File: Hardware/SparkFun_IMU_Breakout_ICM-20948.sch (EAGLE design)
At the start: 37 parts, among them U1 -VFQFN_20, U2 9DoF IMU, U3 1.8V/100mA

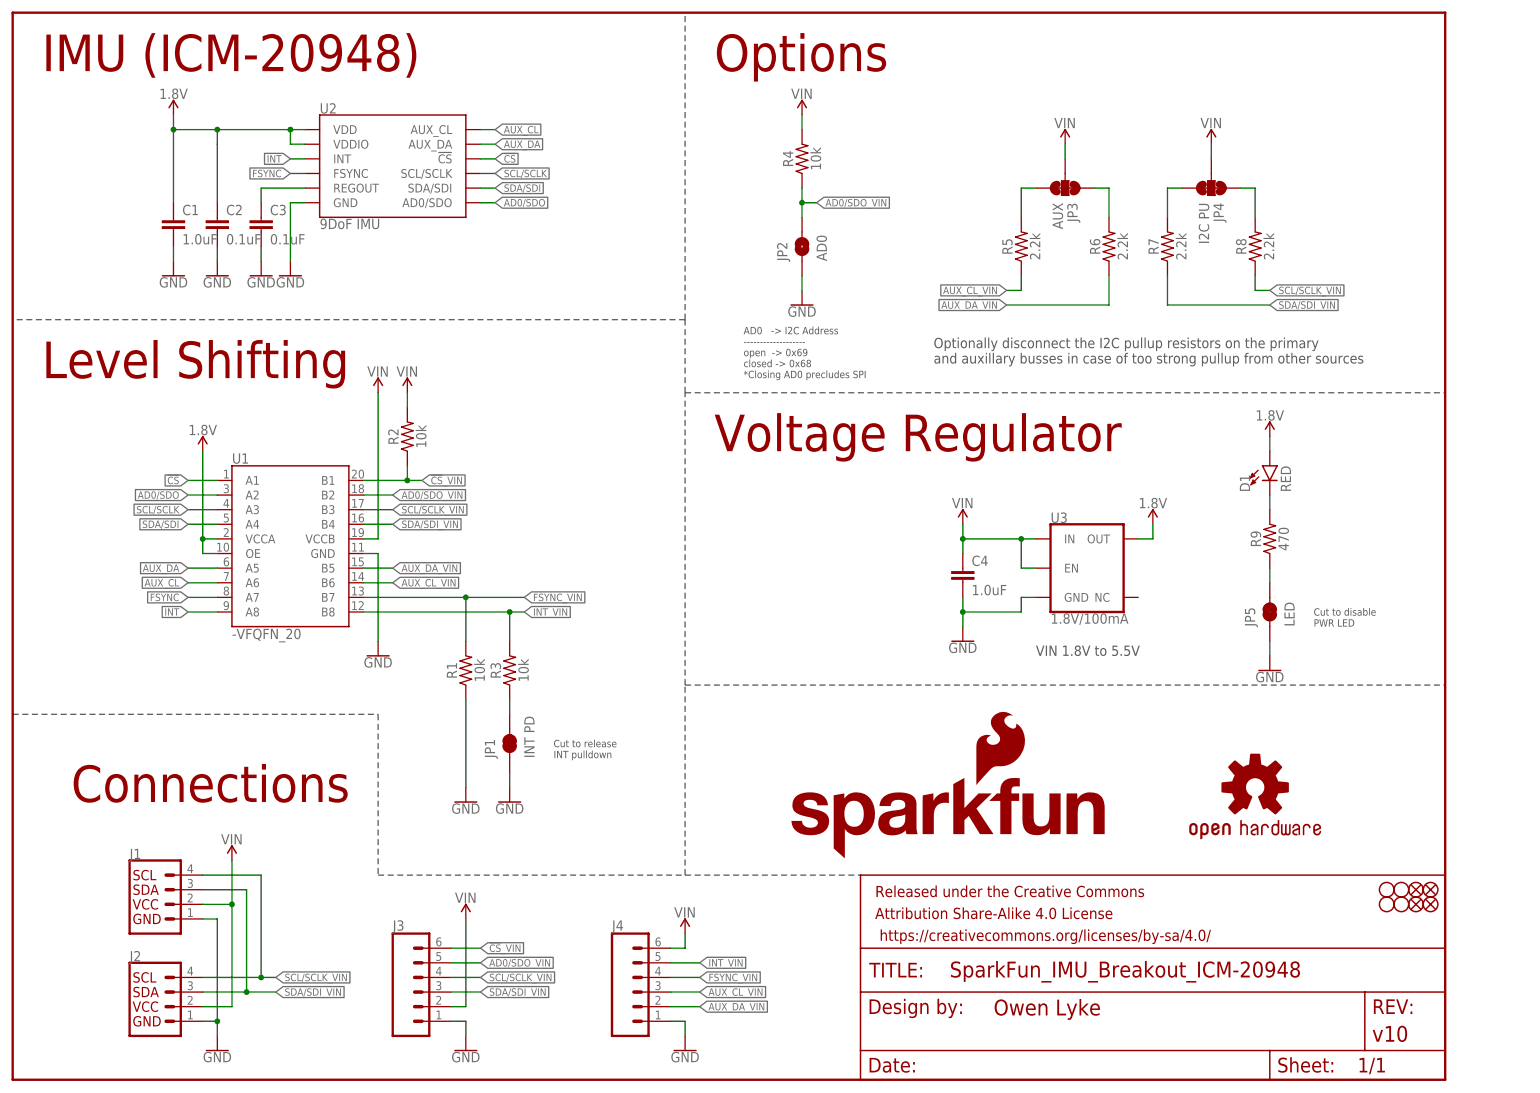
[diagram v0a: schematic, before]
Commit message: v20
v20 is intended to fix the I2C communications. We've identified that the TXB0108 logic level translation IC was unable to drive open-drain busses. To address this we've replaced that IC with the TXS0108 - a very similar chip that IS able to drive open-drain busses.
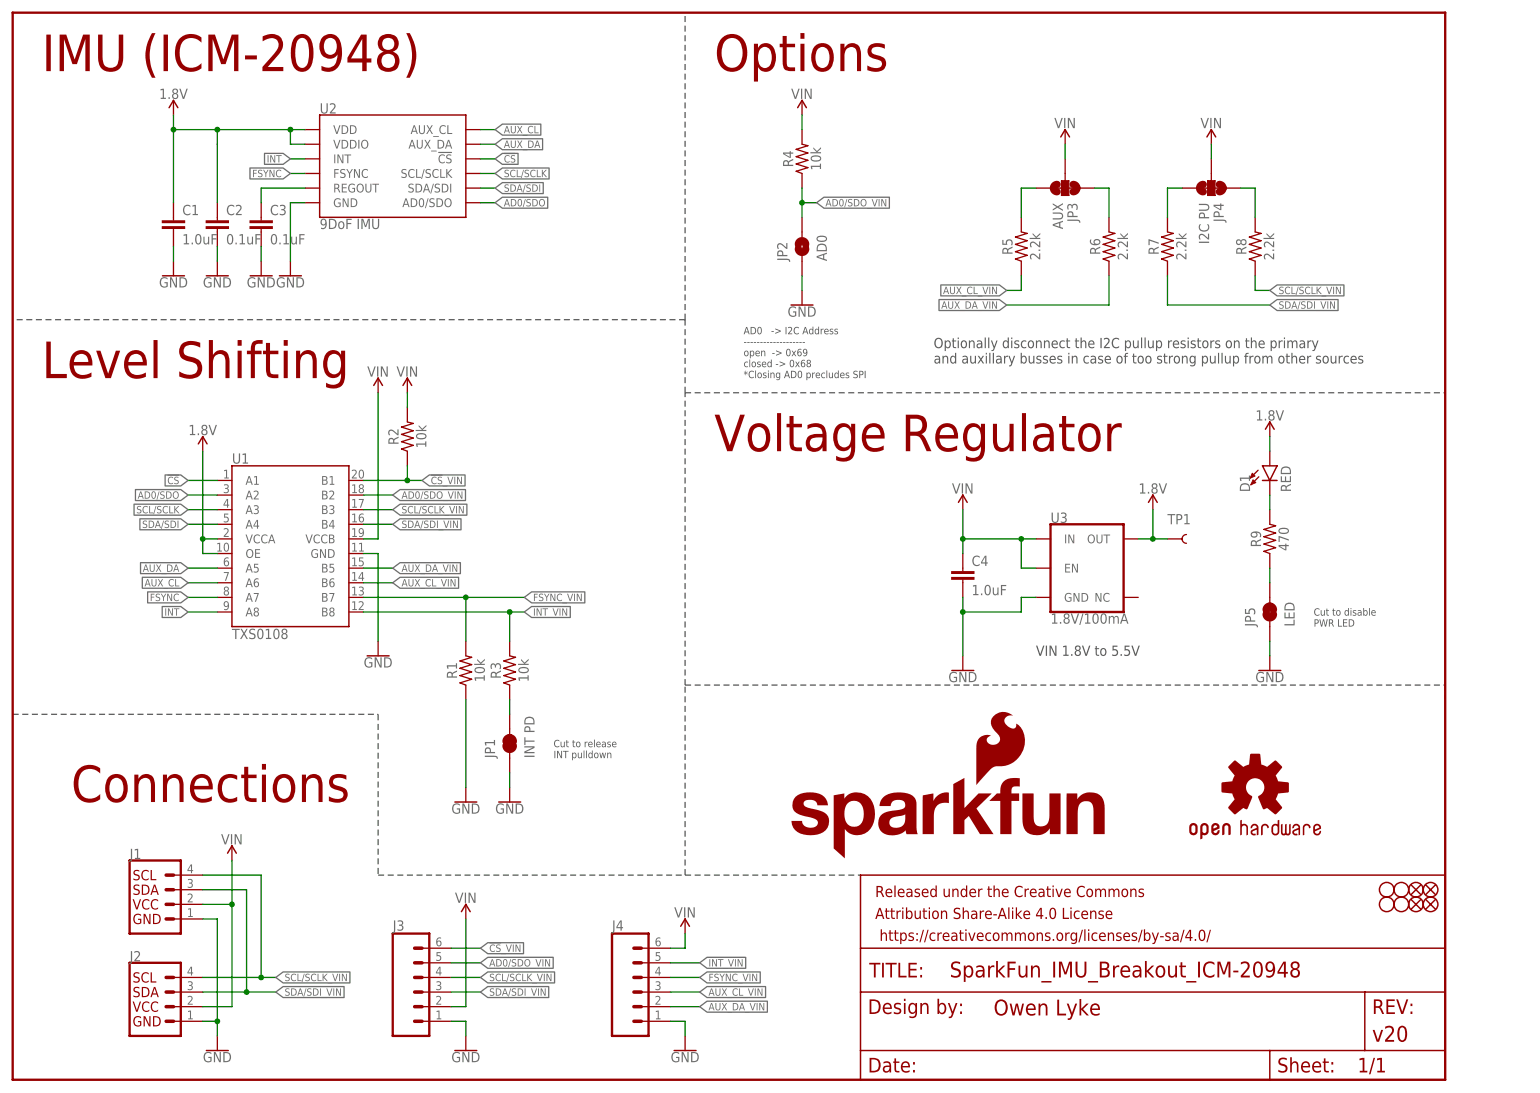
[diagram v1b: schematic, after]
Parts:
- added TP1: 1.8V, SparkFun-Connectors:TEST-POINT3
- FRAME1: REV v10 -> v20
- U1: value -VFQFN_20 -> TXS0108
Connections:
- net 1.8V: now also TP1.1

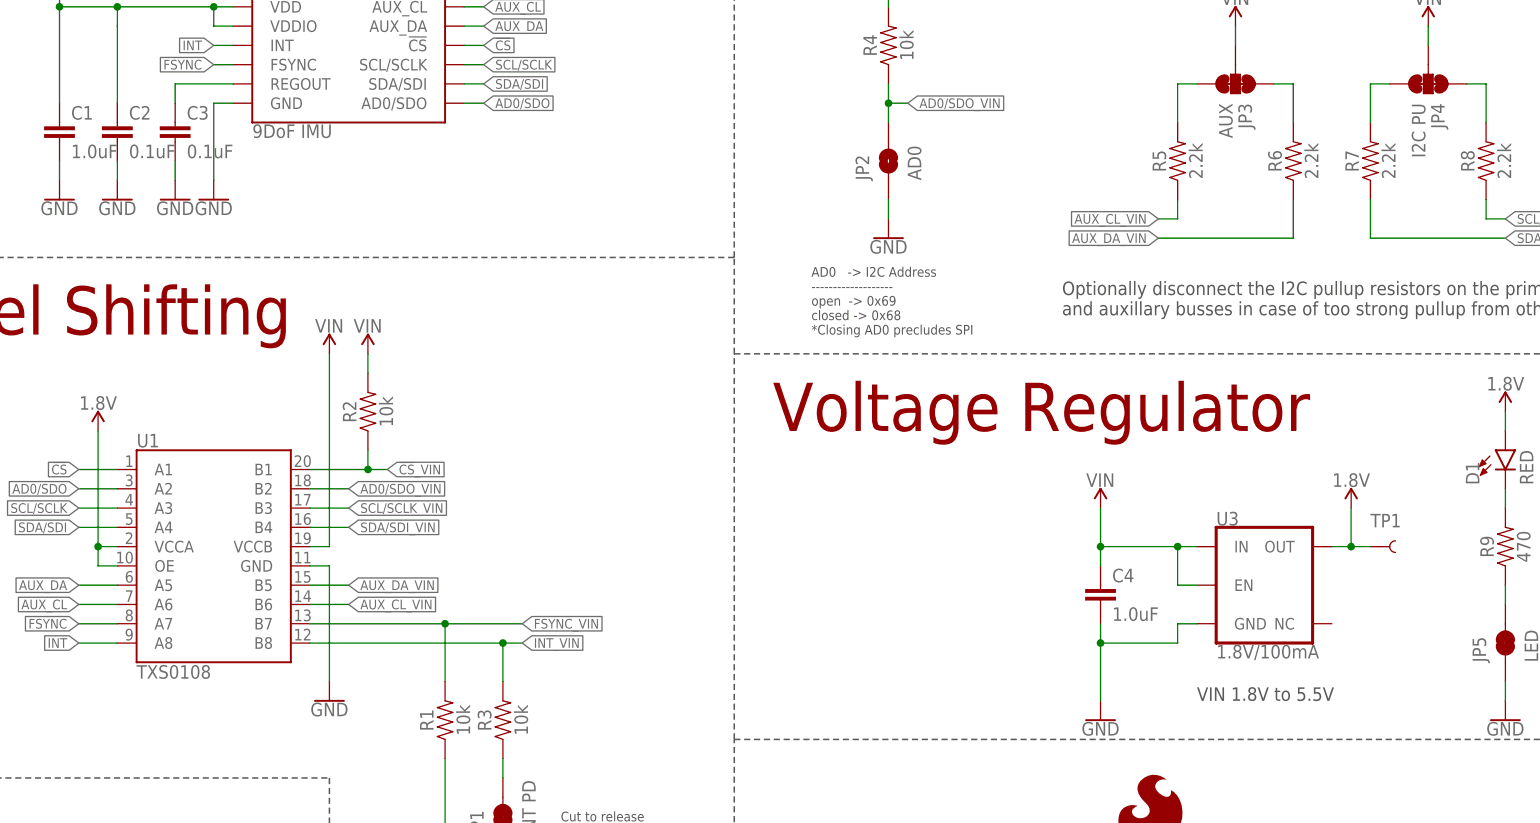
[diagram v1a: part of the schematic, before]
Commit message: Post design review changes for v20
- PWR silk changed to text only
- Moved P1 indicator on ICM-20948
- I<sup>2<\sup>C
- AD0 -> ADR
- No more '0' label for ADR
- Vin range double checked
- GND label on top left
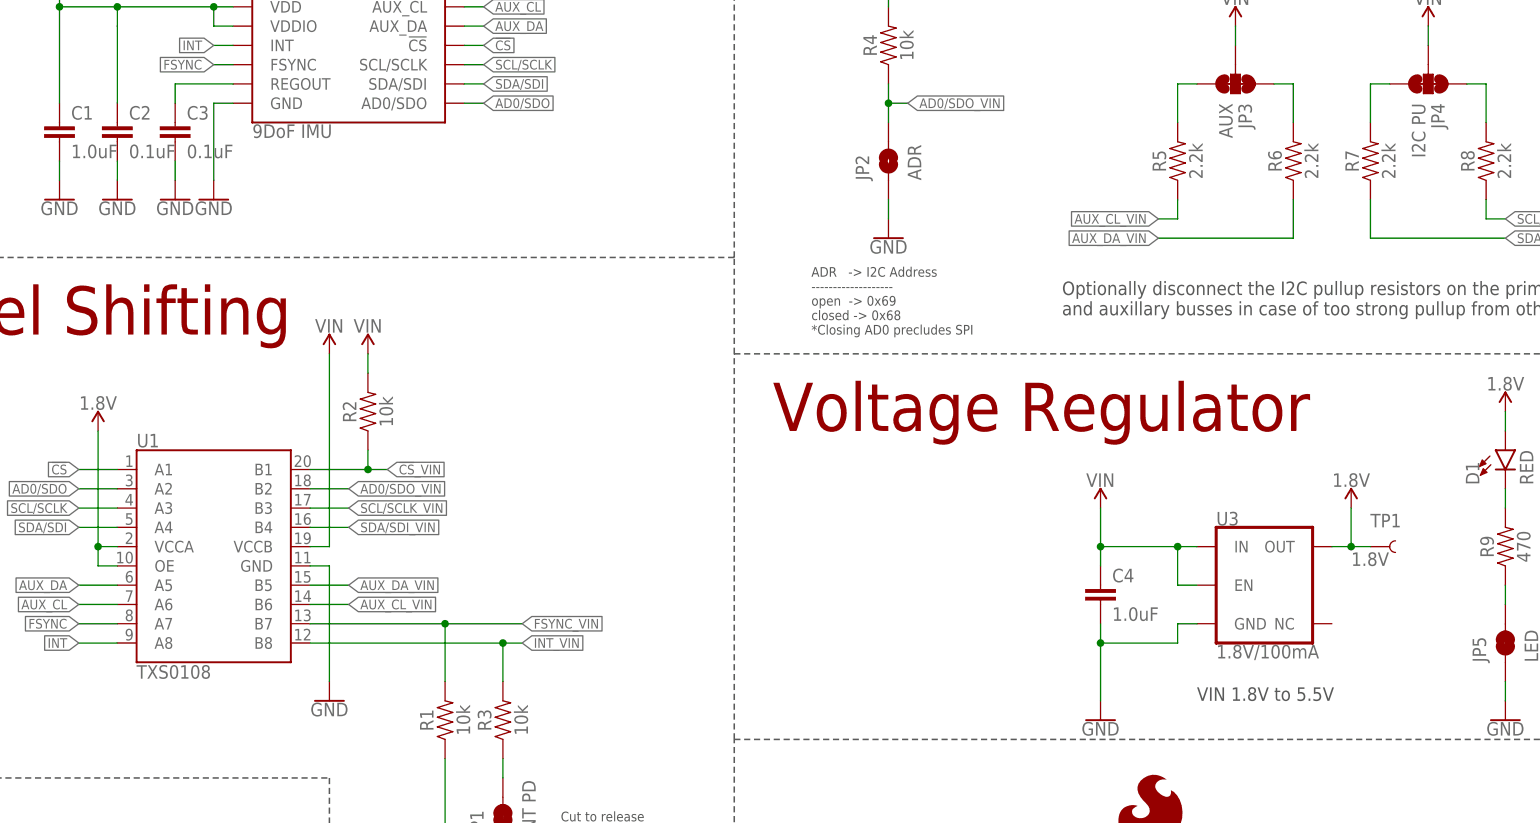
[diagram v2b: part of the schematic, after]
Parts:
- JP2: value AD0 -> ADR
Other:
- note added: "ADR -> I2C Address ------------------- open -> 0x69 closed -> 0x68 *Closing AD0 precludes SPI"
- note removed: "AD0 -> I2C Address ------------------- open -> 0x69 closed -> 0x68 *Closing AD0 precludes SPI"

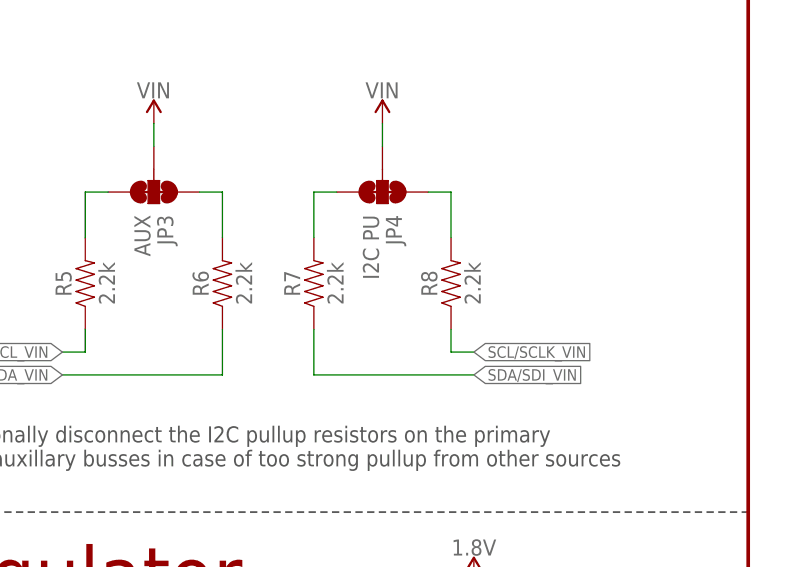
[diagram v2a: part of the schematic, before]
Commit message: Fix I2C Pullup Issue
The combination of pullup resistors on the breakout, within the TXS0108, and on the BlackBoard Qwiic Level shifter conspired to make it impossible for the ICM to pull the data line low.

Fix is to rely on only the internal pullup resistors within the TXS0108.

Also removed a stray silk item from the board
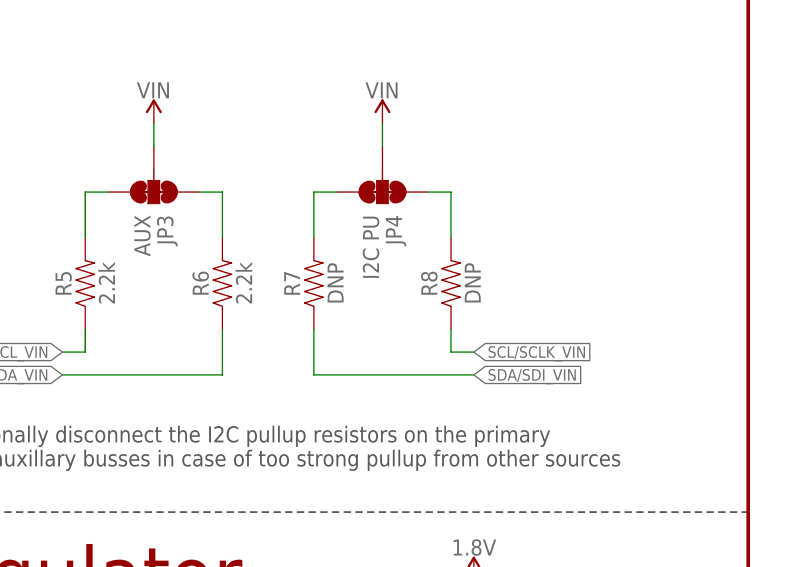
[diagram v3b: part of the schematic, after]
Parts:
- R7, R8: value 2.2k -> DNP; device SparkFun-Resistors:2.2KOHM-0603-1/10W-1% -> SparkFun-Resistors:RESISTOR0603
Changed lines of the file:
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@@
 <?xml version="1.0" encoding="utf-8"?>
 <!DOCTYPE eagle SYSTEM "eagle.dtd">
-<eagle version="9.2.0">
+<eagle version="9.1.3">
 <drawing>
 <settings>
-<setting alwaysvectorfont="no"/>
+<setting alwaysvectorfont="yes"/>
 <setting verticaltext="up"/>
 </settings>
@@
 <part name="GND10" library="SparkFun-PowerSymbols" deviceset="GND" device=""/>
 <part name="R1" library="SparkFun-Resistors" deviceset="10KOHM" device="-0603-1/10W-1%" value="10k"/>
-<part name="R7" library="SparkFun-Resistors" deviceset="2.2KOHM" device="-0603-1/10W-1%" value="2.2k"/>
-<part name="R8" library="SparkFun-Resistors" deviceset="2.2KOHM" device="-0603-1/10W-1%" value="2.2k"/>
+<part name="R7" library="SparkFun-Resistors" deviceset="RESISTOR" device="0603" value="DNP"/>
+<part name="R8" library="SparkFun-Resistors" deviceset="RESISTOR" device="0603" value="DNP"/>
 <part name="R5" library="SparkFun-Resistors" deviceset="2.2KOHM" device="-0603-1/10W-1%" value="2.2k"/>
 <part name="R6" library="SparkFun-Resistors" deviceset="2.2KOHM" device="-0603-1/10W-1%" value="2.2k"/>
